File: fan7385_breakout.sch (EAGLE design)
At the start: 9 parts

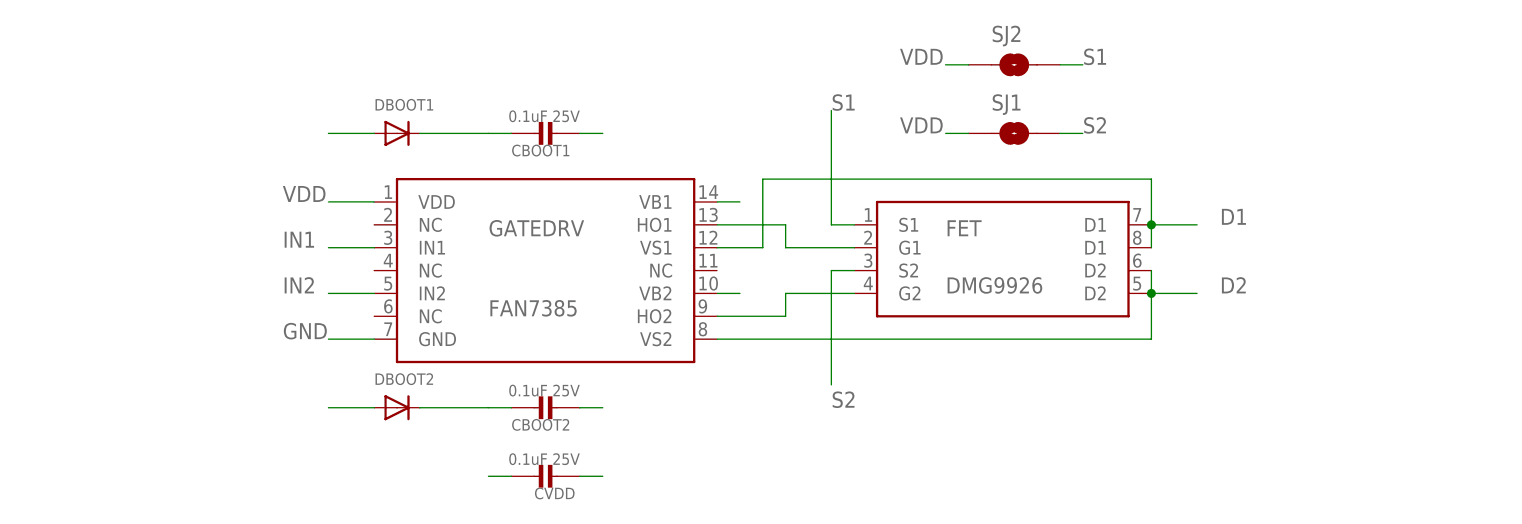
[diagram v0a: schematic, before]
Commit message: added the pin-headers
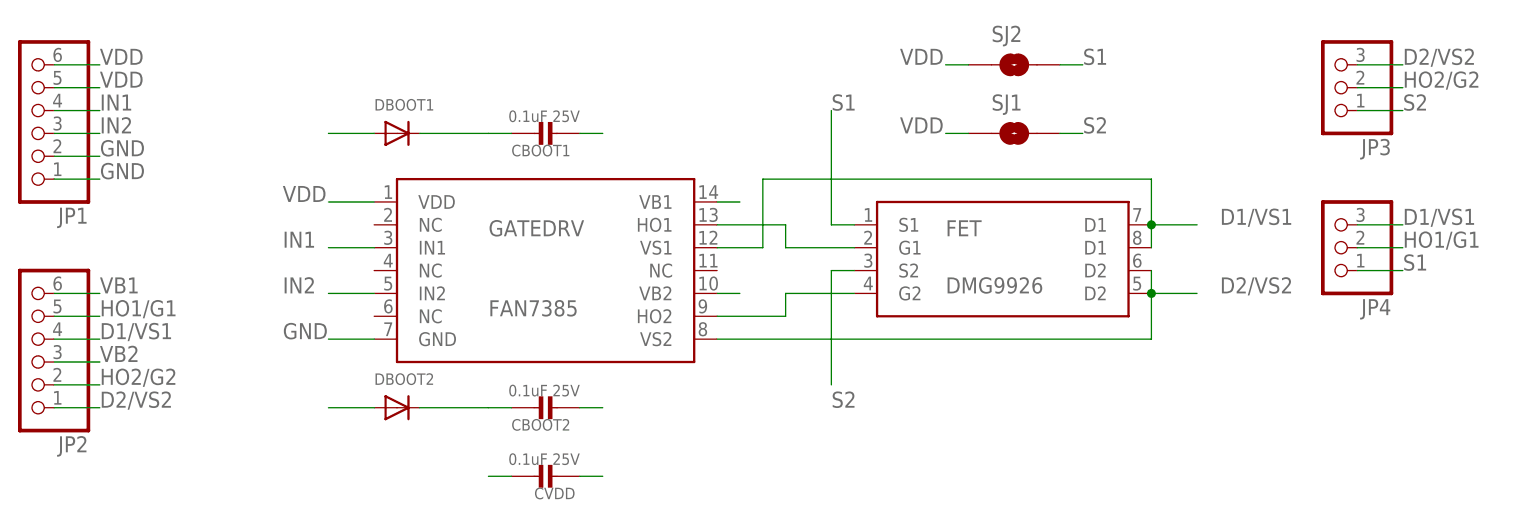
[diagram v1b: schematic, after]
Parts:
- added JP1, JP2: (no value), pinhead:PINHD-1X6
- added JP3, JP4: (no value), pinhead:PINHD-1X3
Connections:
- removed net D1: CBOOT1.P$1, FET.D1@1, FET.D1@2, GATEDRV.VS1
- removed net D2: FET.D2@1, FET.D2@2, GATEDRV.VS2
- removed net PAIR_B_DISCHG_1: CBOOT2.P$1
- new net D1/VS1: CBOOT1.P$1, FET.D1@1, FET.D1@2, GATEDRV.VS1, JP2.4, JP4.3
- new net D2/VS2: CBOOT2.P$1, FET.D2@1, FET.D2@2, GATEDRV.VS2, JP2.1, JP3.3
- net GND: now also JP1.1, JP1.2
- net HO1/G1: now also JP2.5, JP4.2
- net HO2/G2: now also JP2.2, JP3.2
- net IN1: now also JP1.4
- net IN2: now also JP1.3
- net S1: now also JP4.1
- net S2: now also JP3.1
- net VB1: now also JP2.6
- net VB2: now also JP2.3
- net VDD: now also JP1.5, JP1.6
